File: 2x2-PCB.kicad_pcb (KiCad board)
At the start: 2 copper layers, 66.7 x 38.1 mm, 24 parts, among them SW1 SW_Push, U1 ATmega32U4-AU, Y1 16MHz

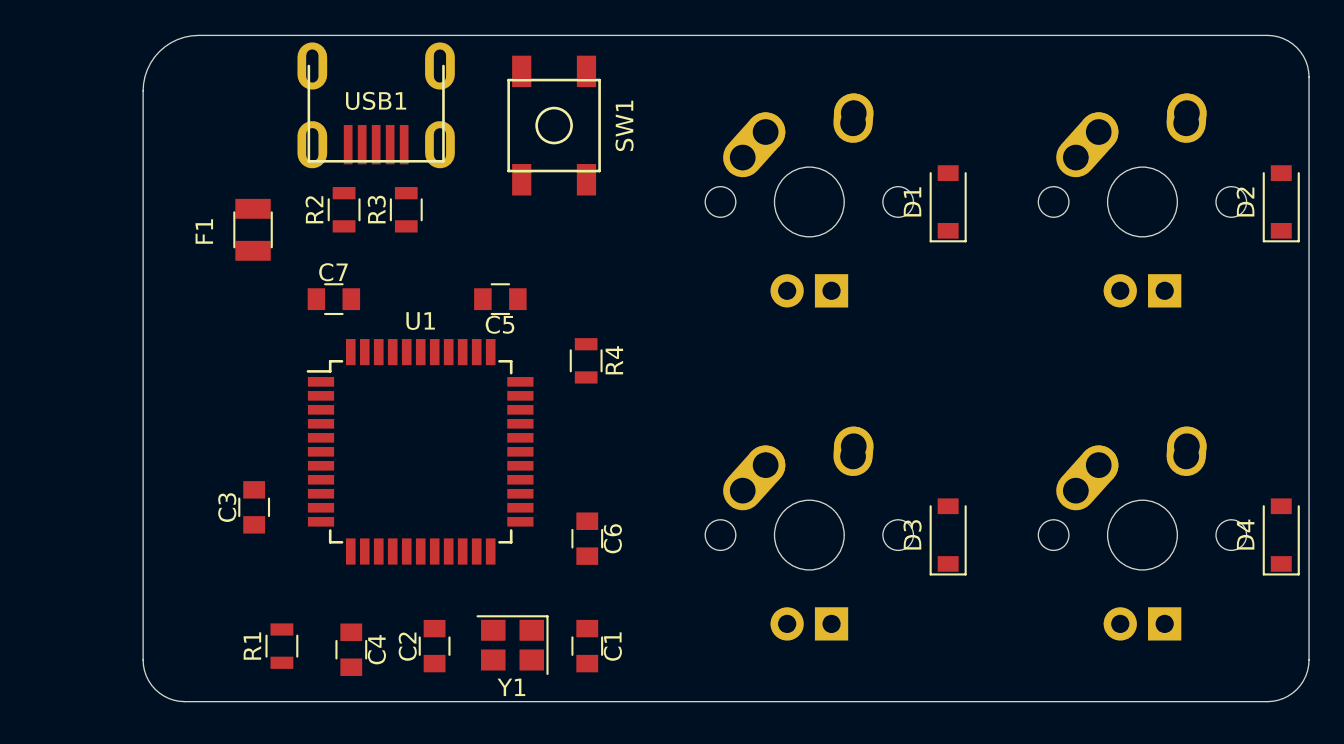
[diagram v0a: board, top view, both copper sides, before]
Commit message: untangled design - ready for tracks
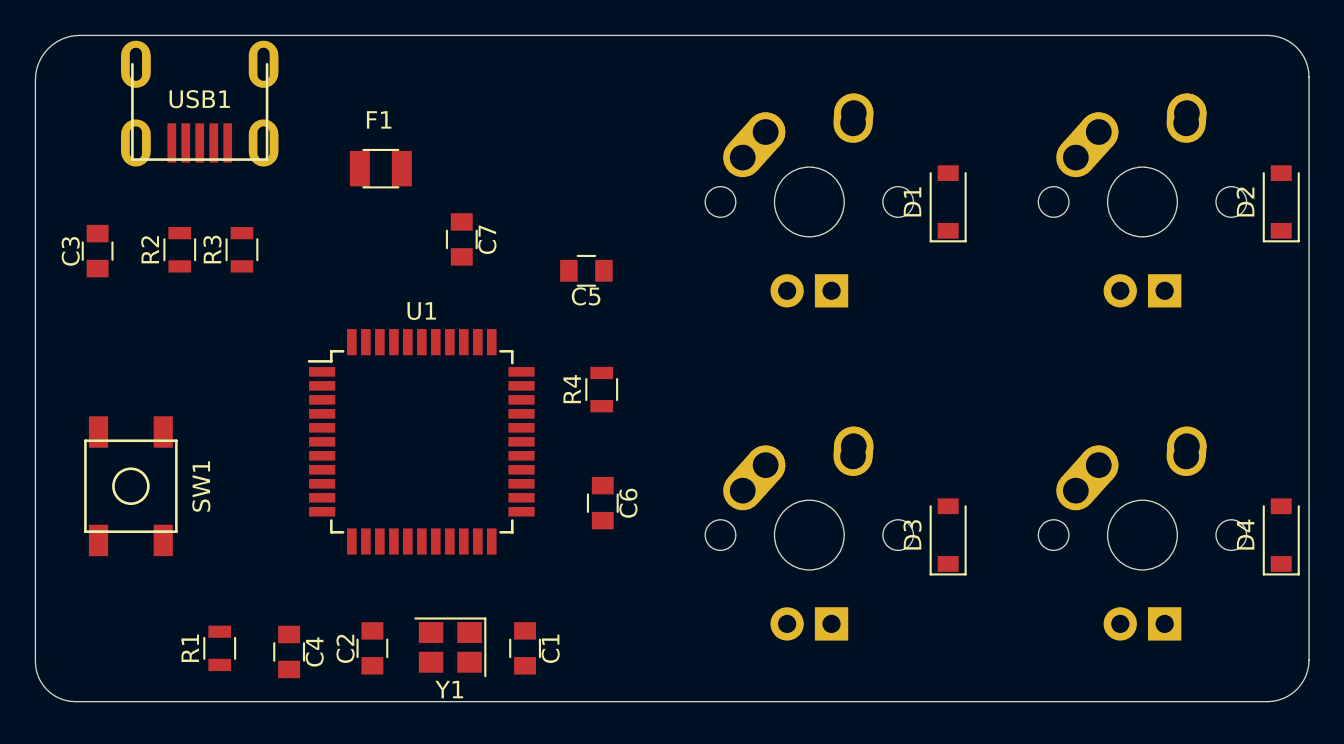
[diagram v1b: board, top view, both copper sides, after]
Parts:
- moved SW1 31.8 mm to (185.0, 105.2)
- moved C3 17.2 mm to (183.1, 91.7)
- moved USB1 10.1 mm to (189.0, 81.0)
- moved R2 9.67 mm to (187.8, 91.6)
- moved R3 9.67 mm to (191.4, 91.6)
- moved F1 8.10 mm to (199.3, 87.0), turned to 0 degrees
- moved C7 8.08 mm to (204.0, 91.0), turned to 270 degrees
- moved C5 5.18 mm to (211.1, 92.8)
- moved C2 3.56 mm to (198.9, 114.4)
- moved C4 3.56 mm to (194.1, 114.6)
- moved R1 3.56 mm to (190.1, 114.4)
- moved Y1 3.56 mm to (203.3, 114.4)
- moved C1 3.56 mm to (207.6, 114.4)
- moved C6 2.22 mm to (212.0, 106.1)
- moved R4 1.87 mm to (212.0, 99.6), turned to 90 degrees
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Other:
- board size 66.7 x 38.1 mm -> 72.8 x 38.1 mm

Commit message: re-organized - no tracks yet
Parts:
- C1, C2, C3, C4, C5, C6, C7, F1, R1, R2, R3, R4, SW1, U1, USB1, Y1: moved to B.Cu
- moved C2 30.1 mm to (202.8, 84.6), turned to 270 degrees
- moved C1 30.1 mm to (211.5, 84.6), turned to 90 degrees
- moved Y1 30.0 mm to (207.2, 84.6)
- moved C4 24.3 mm to (198.8, 90.8), turned to 90 degrees
- moved R1 24.3 mm to (195.5, 90.7), turned to 270 degrees
- moved F1 20.6 mm to (182.5, 98.8), turned to 90 degrees
- moved C7 19.0 mm to (192.4, 106.2), turned to 90 degrees
- moved C5 17.6 mm to (207.3, 110.0)
- moved C3 12.1 mm to (191.7, 100.3), turned to 180 degrees
- moved C6 10.9 mm to (211.6, 95.2), turned to 90 degrees
- moved SW1 7.80 mm to (186.7, 112.8), turned to 180 degrees
- moved R4 7.02 mm to (211.3, 106.6)
- moved R3 5.01 mm to (186.4, 90.9)
- moved R2 2.29 mm to (190.0, 90.9)
- moved U1 1.78 mm to (201.8, 100.8)
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
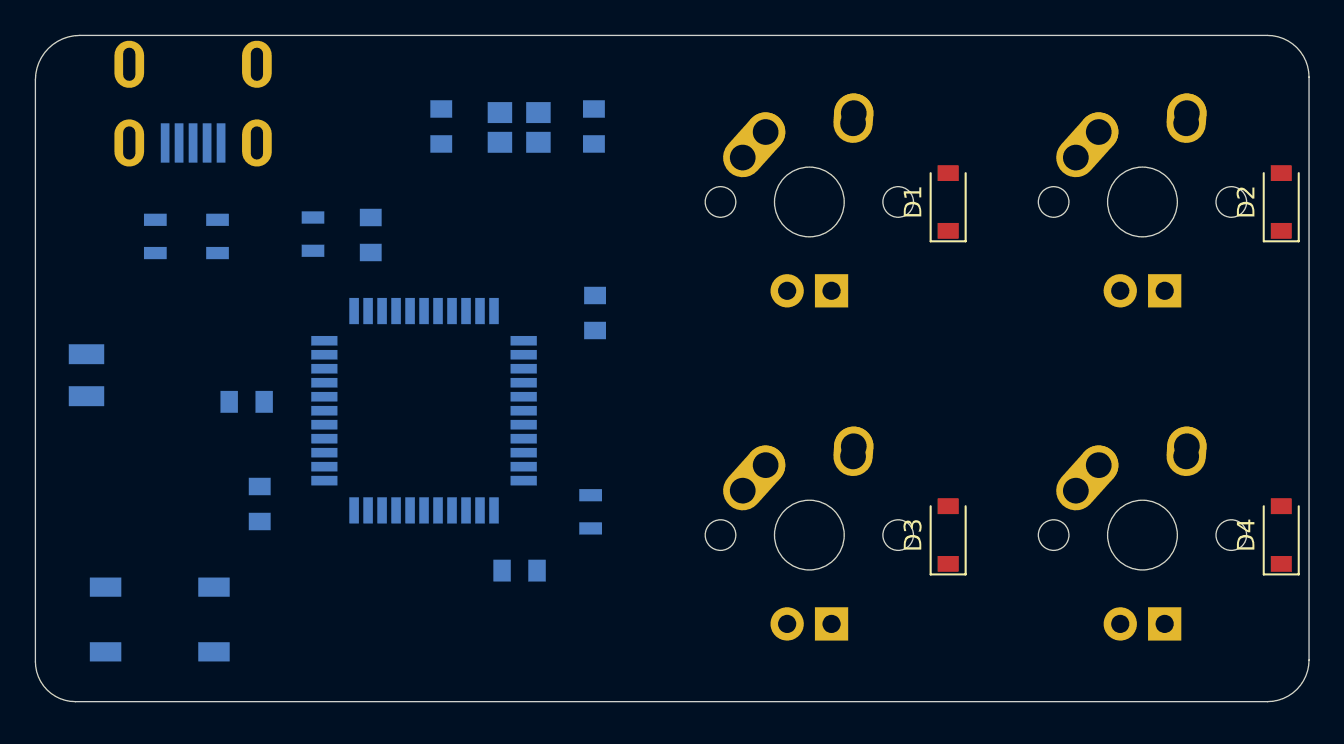
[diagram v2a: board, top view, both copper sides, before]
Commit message: added tracks and traces
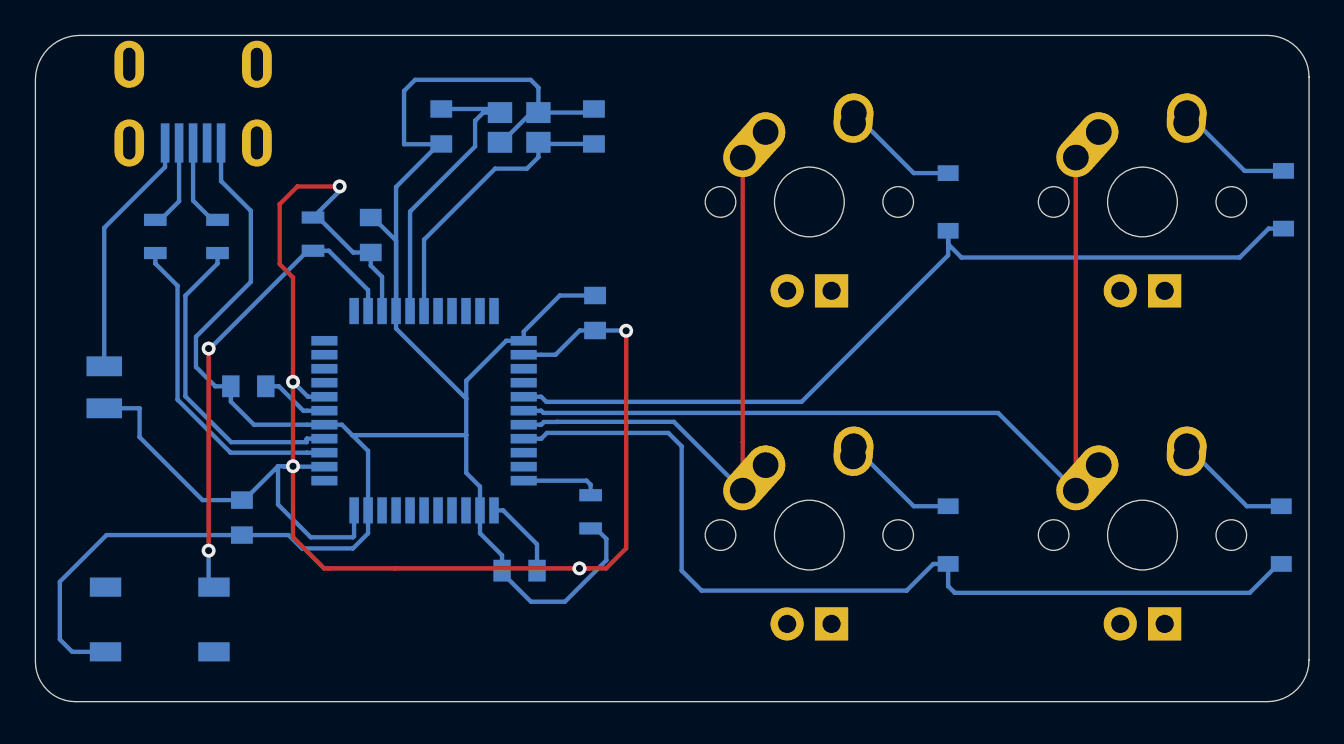
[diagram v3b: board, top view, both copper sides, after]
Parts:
- D1, D2, D3, D4: moved to B.Cu
- moved C7 1.28 mm to (191.4, 107.0), turned to 270 degrees
- moved F1 1.23 mm to (183.5, 99.5), turned to 270 degrees
- moved C3 0.89 mm to (191.8, 99.4)
- moved D2 0.18 mm to (251.0, 88.8)
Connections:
- U1 pad 27: Net-(U1-Pad27) -> ROW0
- U1 pad 28: Net-(U1-Pad28) -> COL1
- U1 pad 29: Net-(U1-Pad29) -> COL0
- U1 pad 30: Net-(U1-Pad30) -> ROW1
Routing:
- net GND: track 0.00 -> 139.7 mm
- net +5V: track 0.00 -> 107.8 mm, vias 0 -> 5
- net ROW1: track 0.00 -> 54.1 mm
- net COL1: track 0.00 -> 52.5 mm
- net ROW0: track 0.00 -> 50.2 mm
- net COL0: track 0.00 -> 33.3 mm
- net Net-(R1-Pad2): track 0.00 -> 27.3 mm, vias 0 -> 2
- net Net-(R3-Pad1): track 0.00 -> 18.6 mm
- net Net-(R2-Pad1): track 0.00 -> 18.2 mm
- net Net-(C2-Pad1): track 0.00 -> 17.5 mm
- net Net-(C1-Pad1): track 0.00 -> 16.6 mm
- net VCC: track 0.00 -> 14.2 mm
- net Net-(D2-Pad2): track 0.00 -> 6.89 mm
- net Net-(D3-Pad2): track 0.00 -> 6.82 mm
- net Net-(D1-Pad2): track 0.00 -> 6.75 mm
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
